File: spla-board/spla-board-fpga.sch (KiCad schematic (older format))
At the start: 44 parts, among them J2 J_JTAG, U1 LFE5U-45F-BG256, U4 74LVC1G17, U5 74LVC1G17

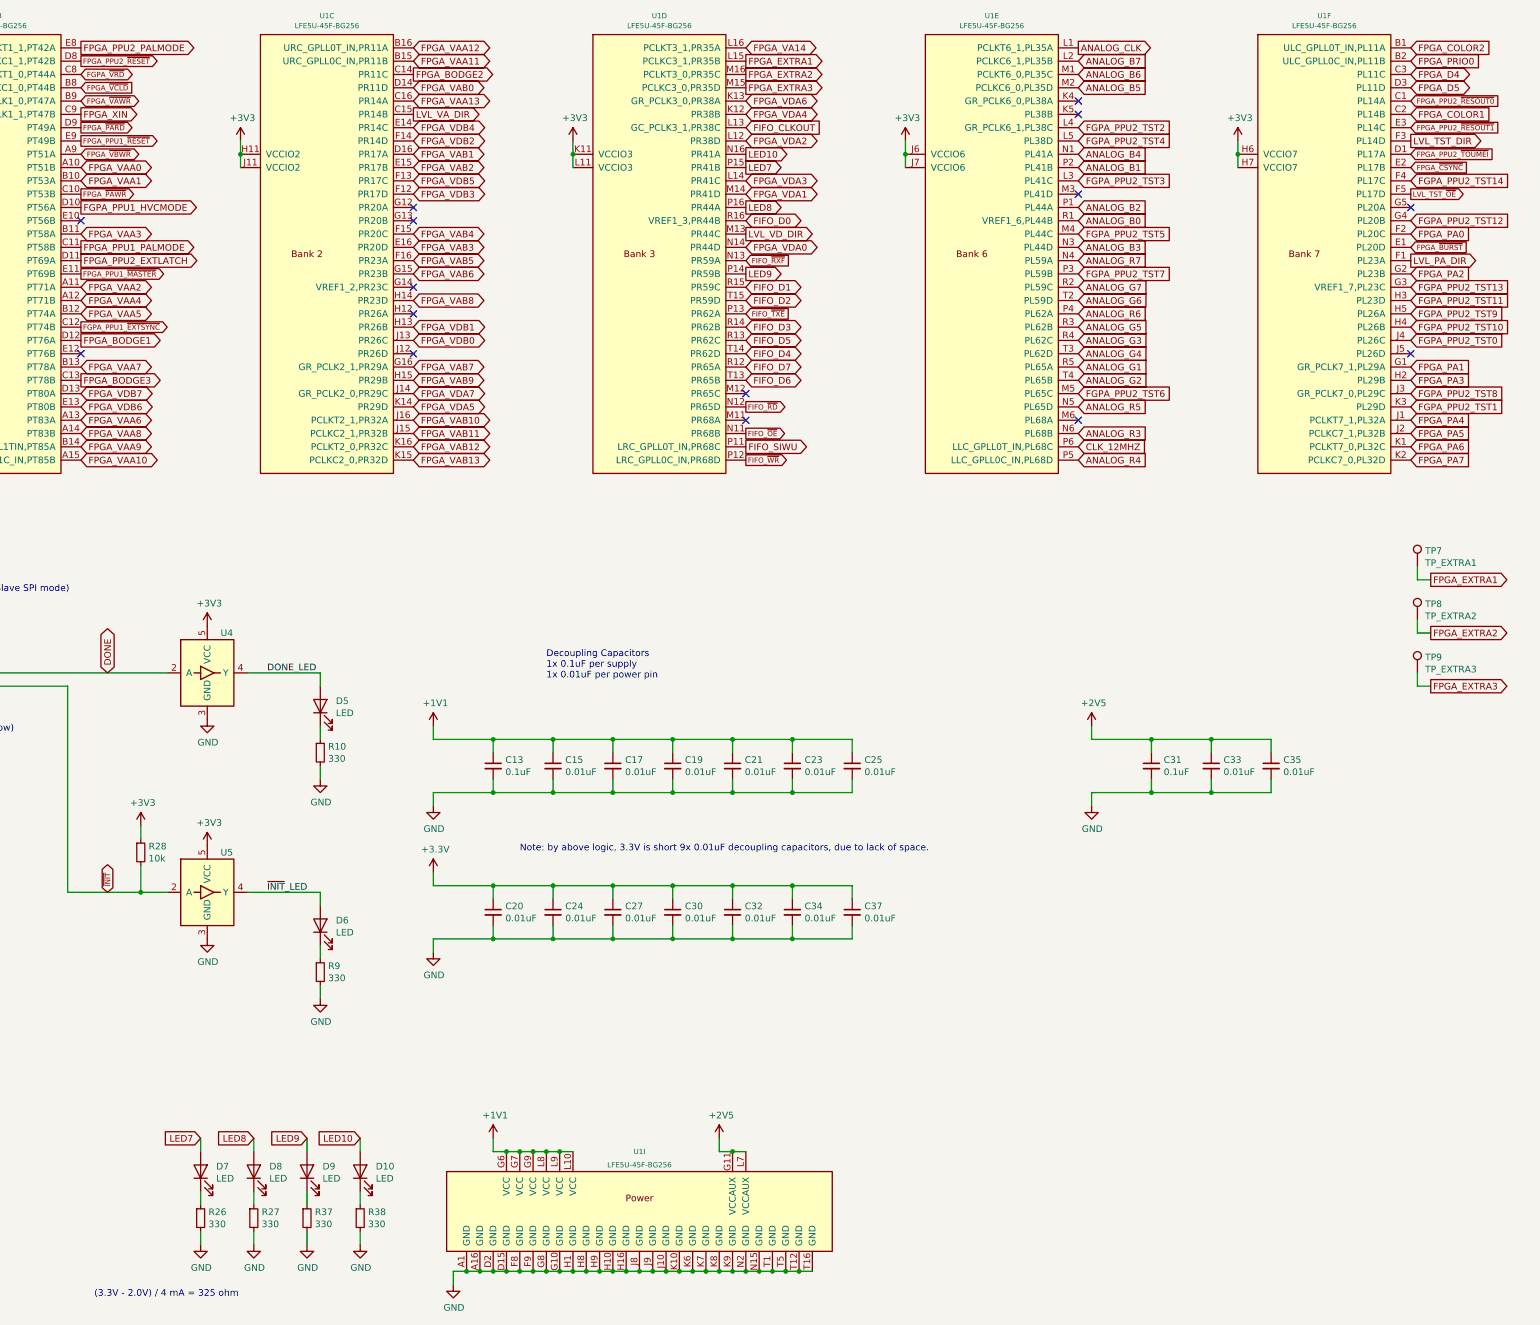
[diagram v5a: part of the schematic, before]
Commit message: schematic/pcb: Swap test points for pins; Rename LEDs.
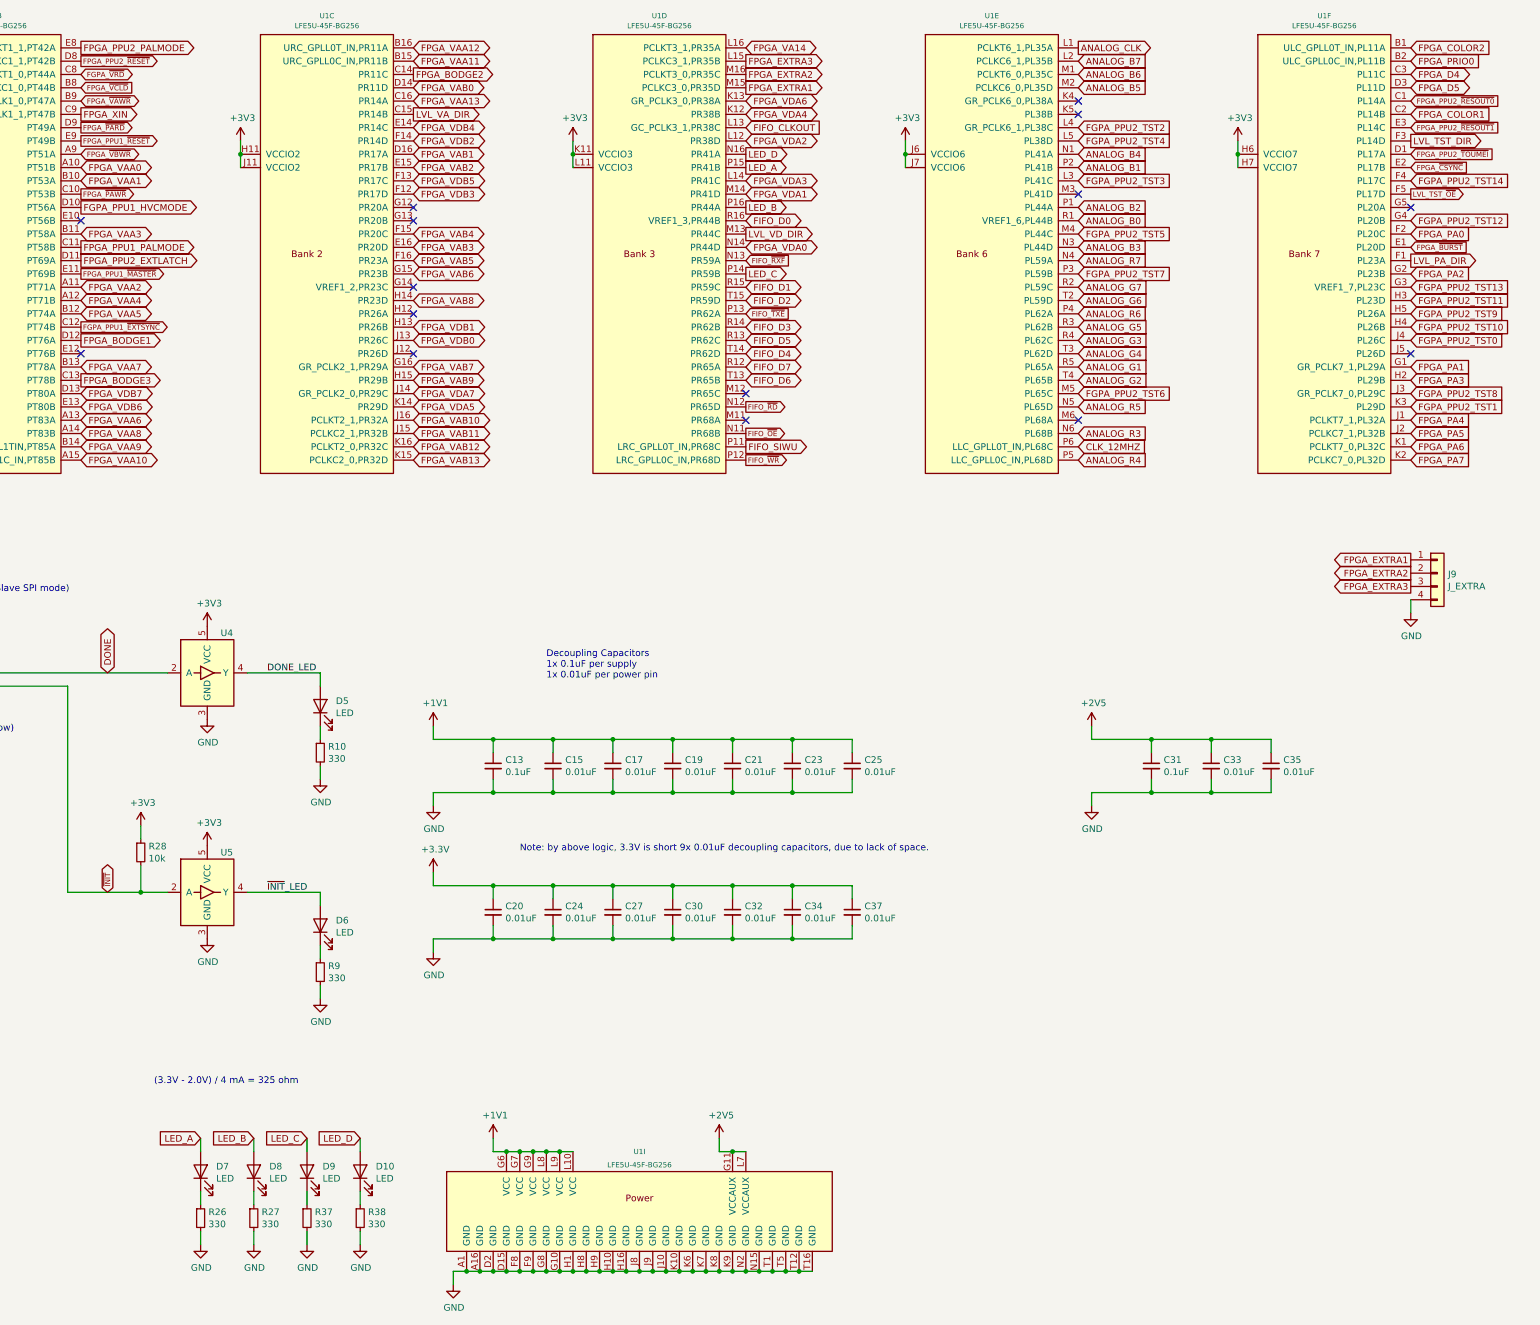
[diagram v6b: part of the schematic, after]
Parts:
- removed TP7: TP_EXTRA1, TestPoint:TestPoint_Pad_D2.0mm, symbol Connector:TestPoint
- removed TP8: TP_EXTRA2, TestPoint:TestPoint_Pad_D2.0mm, symbol Connector:TestPoint
- removed TP9: TP_EXTRA3, TestPoint:TestPoint_Pad_D2.0mm, symbol Connector:TestPoint
- added J9: J_EXTRA, Connector_PinHeader_2.54mm:PinHeader_1x04_P2.54mm_Vertical, symbol Connector_Generic:Conn_01x04
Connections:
- net FPGA_EXTRA1: now also U1.M15 (PCLKC3_0,PR35D), J9.1 (Pin_1); no longer U1.L15 (PCLKC3_1,PR35B)
- net FPGA_EXTRA2: now also J9.2 (Pin_2)
- net FPGA_EXTRA3: now also U1.L15 (PCLKC3_1,PR35B), J9.3 (Pin_3); no longer U1.M15 (PCLKC3_0,PR35D)
- net GND: now also J9.4 (Pin_4)
- net LED10 renamed LED_D
- net LED7 renamed LED_A
- net LED8 renamed LED_B
- net LED9 renamed LED_C
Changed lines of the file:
@@
 	1    0    0    -1
 $EndComp
-Text Notes 4750 10700 0    50   ~ 0
+Text Notes 5200 9100 0    50   ~ 0
 (3.3V - 2.0V) / 4 mA = 325 ohm
 Wire Wire Line
 	5950 9500 5950 9600
 Text GLabel 5550 9500 0    50   Input ~ 0
-LED7
+LED_A
 Text GLabel 5950 9500 0    50   Input ~ 0
-LED8
+LED_B
 Text GLabel 9650 2200 2    50   Output ~ 0
-LED7
-Text GLabel 9650 2500 2    50   Output ~ 0
-LED8
+LED_A
 NoConn ~ 9650 4100
 NoConn ~ 9650 3900
@@
 Text Notes 7950 7350 0    50   ~ 0
 Note: by above logic, 3.3V is short 9x 0.01uF decoupling capacitors, due to lack of space.
-Text GLabel 9650 1400 2    50   Output ~ 0
+Text GLabel 9650 1600 2    50   Output ~ 0
 FPGA_EXTRA1
 Text GLabel 9650 1500 2    50   Output ~ 0
 FPGA_EXTRA2
-Text GLabel 9650 1600 2    50   Output ~ 0
+Text GLabel 9650 1400 2    50   Output ~ 0
 FPGA_EXTRA3
-Text GLabel 14800 5300 2    50   Output ~ 0
+Text GLabel 14650 5150 0    50   Output ~ 0
 FPGA_EXTRA1
-Text GLabel 14800 5700 2    50   Output ~ 0
+Text GLabel 14650 5250 0    50   Output ~ 0
 FPGA_EXTRA2
-Text GLabel 14800 6100 2    50   Output ~ 0
+Text GLabel 14650 5350 0    50   Output ~ 0
 FPGA_EXTRA3
-$Comp
-L Connector:TestPoint TP7
-U 1 1 5EA65145
-P 14700 5200
-F 0 "TP7" H 14758 5318 50  0000 L CNN
-F 1 "TP_EXTRA1" H 14758 5227 50  0000 L CNN
-F 2 "TestPoint:TestPoint_Pad_D2.0mm" H 14900 5200 50  0001 C CNN
-F 3 "~" H 14900 5200 50  0001 C CNN
-F 4 "N/A" H 14700 5200 50  0001 C CNN "Digikey"
-F 5 "N/A" H 14700 5200 50  0001 C CNN "Manufacturer Id"
-F 6 "N/A" H 14700 5200 50  0001 C CNN "Manufacturer"
-	1    14700 5200
-	1    0    0    -1
-$EndComp
-$Comp
-L Connector:TestPoint TP8
-U 1 1 5EA6567A
-P 14700 5600
-F 0 "TP8" H 14758 5718 50  0000 L CNN
-F 1 "TP_EXTRA2" H 14758 5627 50  0000 L CNN
-F 2 "TestPoint:TestPoint_Pad_D2.0mm" H 14900 5600 50  0001 C CNN
-F 3 "~" H 14900 5600 50  0001 C CNN
-F 4 "N/A" H 14700 5600 50  0001 C CNN "Digikey"
-F 5 "N/A" H 14700 5600 50  0001 C CNN "Manufacturer Id"
-F 6 "N/A" H 14700 5600 50  0001 C CNN "Manufacturer"
-	1    14700 5600
-	1    0    0    -1
-$EndComp
-$Comp
-L Connector:TestPoint TP9
-U 1 1 5EA6C737
-P 14700 6000
-F 0 "TP9" H 14758 6118 50  0000 L CNN
-F 1 "TP_EXTRA3" H 14758 6027 50  0000 L CNN
-F 2 "TestPoint:TestPoint_Pad_D2.0mm" H 14900 6000 50  0001 C CNN
-F 3 "~" H 14900 6000 50  0001 C CNN
-F 4 "N/A" H 14700 6000 50  0001 C CNN "Digikey"
-F 5 "N/A" H 14700 6000 50  0001 C CNN "Manufacturer Id"
-F 6 "N/A" H 14700 6000 50  0001 C CNN "Manufacturer"
-	1    14700 6000
-	1    0    0    -1
-$EndComp
-Wire Wire Line
-	14800 5300 14700 5300
-Wire Wire Line
-	14700 5300 14700 5200
-Wire Wire Line
-	14800 5700 14700 5700
-Wire Wire Line
-	14700 5700 14700 5600
-Wire Wire Line
-	14800 6100 14700 6100
-Wire Wire Line
-	14700 6100 14700 6000
 Wire Wire Line
 	3000 6700 2800 6700
@@
 	6750 9500 6750 9600
 Text GLabel 6350 9500 0    50   Input ~ 0
-LED9
+LED_C
 Text GLabel 6750 9500 0    50   Input ~ 0
-LED10
+LED_D
 $Comp
 L Device:LED D?
@@
 Wire Wire Line
 	2900 7800 2900 7850
-Text GLabel 9650 3000 2    50   Output ~ 0
-LED9
 Text GLabel 9650 2100 2    50   Output ~ 0
-LED10
+LED_D
 Wire Wire Line
 	2150 6700 2800 6700
@@
 Wire Wire Line
 	850  5750 850  5850
+$Comp
+L Connector_Generic:Conn_01x04 J?
+U 1 1 5FA04E8A
+P 14850 5250
+AR Path="/5E50D400/5FA04E8A" Ref="J?"  Part="1"
+AR Path="/5E4D8358/5FA04E8A" Ref="J9"  Part="1"
+F 0 "J9" H 14930 5242 50  0000 L CNN
+F 1 "J_EXTRA" H 14930 5151 50  0000 L CNN
+F 2 "Connector_PinHeader_2.54mm:PinHeader_1x04_P2.54mm_Vertical" H 14850 5250 50  0001 C CNN
+F 3 "~" H 14850 5250 50  0001 C CNN
+F 4 "S1011EC-40-ND" H 14850 5250 50  0001 C CNN "Digikey"
+F 5 "PRPC040SAAN-RC" H 14850 5250 50  0001 C CNN "Manufacturer Id"
+F 6 "Sullins Connector Solutions" H 14850 5250 50  0001 C CNN "Manufacturer"
+	1    14850 5250
+	1    0    0    -1
+$EndComp
+$Comp
+L power:GND #PWR0244
+U 1 1 5FA509E2
+P 14650 5550
+F 0 "#PWR0244" H 14650 5300 50  0001 C CNN
+F 1 "GND" H 14655 5377 50  0000 C CNN
+F 2 "" H 14650 5550 50  0001 C CNN
+F 3 "" H 14650 5550 50  0001 C CNN
+	1    14650 5550
+	1    0    0    -1
+$EndComp
+Wire Wire Line
+	14650 5450 14650 5550
+Text GLabel 9650 3000 2    50   Output ~ 0
+LED_C
+Text GLabel 9650 2500 2    50   Output ~ 0
+LED_B
 $EndSCHEMATC

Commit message: schematic/pcb: Add a button, for generic use by the FPGA.
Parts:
- added C45: 0.1uF, Capacitor_SMD:C_0603_1608Metric, symbol Device:C
- added R42, R43: 10k, Resistor_SMD:R_0603_1608Metric, symbol Device:R
- added SW1: PTS645, SPLA:PTS645-SMTR92, symbol Switch:SW_Push
- J9: footprint Connector_PinHeader_2.54mm:PinHeader_1x04_P2.54mm_Vertical -> Connector_PinHeader_2.54mm:PinHeader_1x05_P2.54mm_Vertical; symbol Connector_Generic:Conn_01x04 -> Connector_Generic:Conn_01x05
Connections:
- net +3V3: now also SW1.2
- net GND: now also J9.5 (Pin_5), C45.2, R42.2; no longer J9.4 (Pin_4)
- new net: R42.1, R43.2, SW1.1
- new net BUTTON1: C45.1, J9.4 (Pin_4), R43.1
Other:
- note added: "Debounce filter, 0.1uF * 10k ohm = 1ms"
- moved on the sheet: C13, C15, C17, C19, C20, C21, C23, C24, C25, C27, C30, C31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

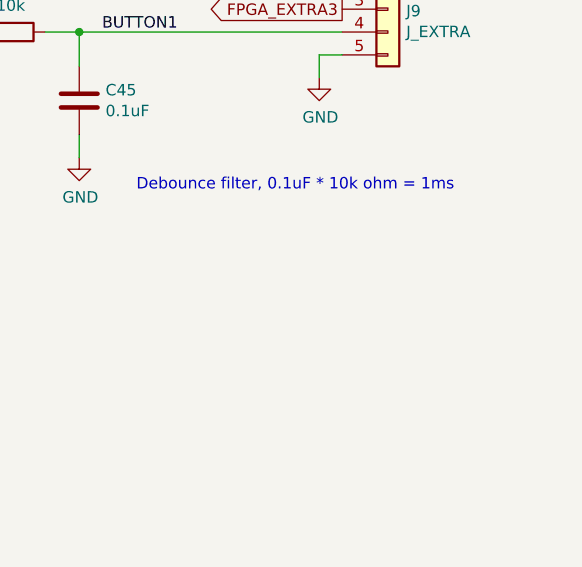
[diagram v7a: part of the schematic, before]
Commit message: schematic/pcb: Add jumper for button.
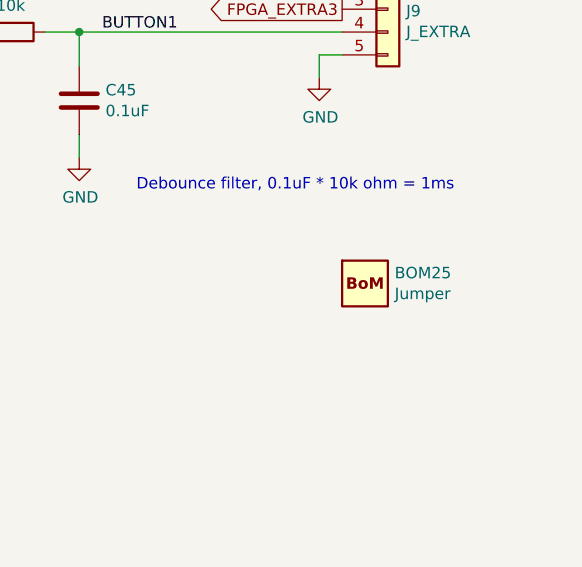
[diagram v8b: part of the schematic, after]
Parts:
- added BOM25: Jumper, SPLA:BoM, symbol SPLA:BomExtra
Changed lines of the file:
@@
 Text Label 13700 6350 0    50   ~ 0
 BUTTON1
+$Comp
+L SPLA:BomExtra BOM?
+U 1 1 5F3CE063
+P 14850 7450
+AR Path="/5E50E589/5F3CE063" Ref="BOM?"  Part="1"
+AR Path="/5E50D39B/5F3CE063" Ref="BOM?"  Part="1"
+AR Path="/5E4D8358/5F3CE063" Ref="BOM25"  Part="1"
+F 0 "BOM25" H 14980 7496 50  0000 L CNN
+F 1 "Jumper" H 14980 7405 50  0000 L CNN
+F 2 "SPLA:BoM" H 14850 7450 50  0001 C CNN
+F 3 "" H 14850 7450 50  0001 C CNN
+F 4 "S9337-ND" H 14850 7450 50  0001 C CNN "Digikey"
+F 5 "QPC02SXGN-RC" H 14850 7450 50  0001 C CNN "Manufacturer Id"
+F 6 "Sullins Connector Solutions" H 14850 7450 50  0001 C CNN "Manufacturer"
+	1    14850 7450
+	1    0    0    -1
+$EndComp
 $EndSCHEMATC
